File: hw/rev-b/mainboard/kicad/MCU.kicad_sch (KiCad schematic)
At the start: 34 parts, among them J23 MENU_HDR, SW4 RUN, SW5 MENU_BTN, U21 RP2040, Y1 12 MHz

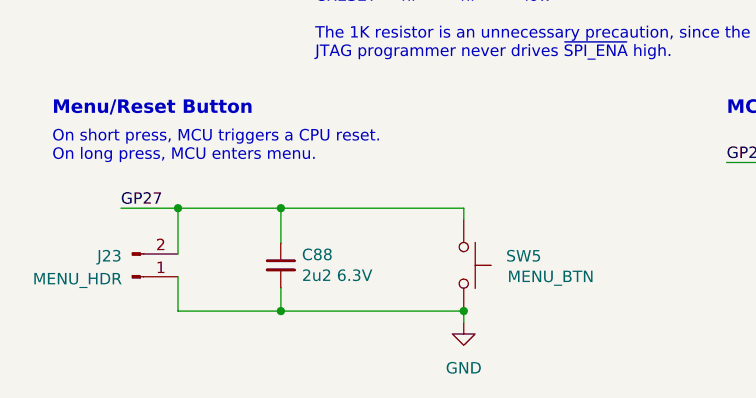
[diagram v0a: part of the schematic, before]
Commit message: hw: move USB-C for 8032SK (WIP)
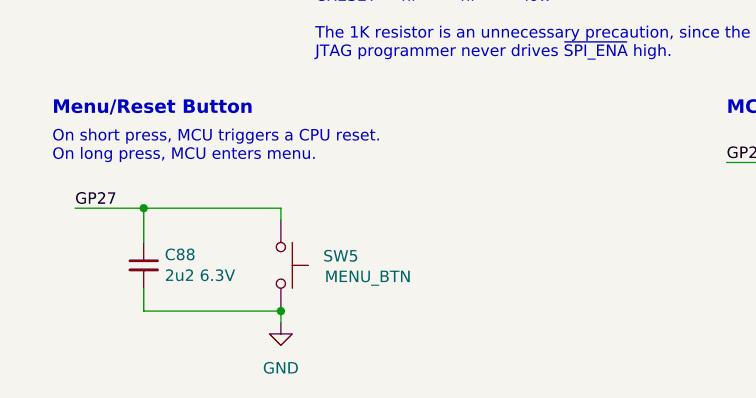
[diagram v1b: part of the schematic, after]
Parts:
- removed J23: MENU_HDR, Connector_PinHeader_2.54mm:PinHeader_1x02_P2.54mm_Vertical, symbol Connector:Conn_01x02_Pin
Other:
- moved on the sheet: C88, SW5
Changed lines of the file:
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@@
 	)
 	(junction
-		(at 44.45 179.07)
+		(at 29.21 179.07)
 		(diameter 0)
 		(color 0 0 0 0)
@@
 	)
 	(junction
-		(at 44.45 190.5)
-		(diameter 0)
-		(color 0 0 0 0)
-	)
-	(junction
 		(at 187.96 59.69)
 		(diameter 0)
@@
 	)
 	(junction
-		(at 64.77 190.5)
+		(at 44.45 190.5)
 		(diameter 0)
 		(color 0 0 0 0)
@@
 	)
 	(junction
-		(at 33.02 179.07)
-		(diameter 0)
-		(color 0 0 0 0)
-	)
-	(junction
 		(at 82.55 31.75)
 		(diameter 0)
@@
 	(wire
 		(pts
-			(xy 33.02 186.69) (xy 33.02 190.5)
-		)
-		(stroke
-			(width 0)
-			(type default)
-		)
-	)
-	(wire
-		(pts
 			(xy 193.04 52.07) (xy 193.04 53.34)
 		)
@@
 	(wire
 		(pts
-			(xy 33.02 190.5) (xy 44.45 190.5)
-		)
-		(stroke
-			(width 0)
-			(type default)
-		)
-	)
-	(wire
-		(pts
 			(xy 133.35 138.43) (xy 133.35 139.7)
 		)
@@
 	(wire
 		(pts
-			(xy 44.45 187.96) (xy 44.45 190.5)
+			(xy 29.21 187.96) (xy 29.21 190.5)
 		)
 		(stroke
@@
 	(wire
 		(pts
-			(xy 44.45 179.07) (xy 64.77 179.07)
+			(xy 29.21 179.07) (xy 44.45 179.07)
 		)
 		(stroke
@@
 	(wire
 		(pts
-			(xy 44.45 179.07) (xy 44.45 182.88)
+			(xy 29.21 179.07) (xy 29.21 182.88)
 		)
 		(stroke
@@
 	(wire
 		(pts
-			(xy 44.45 190.5) (xy 64.77 190.5)
+			(xy 29.21 190.5) (xy 44.45 190.5)
 		)
 		(stroke
@@
 	(wire
 		(pts
-			(xy 33.02 179.07) (xy 44.45 179.07)
+			(xy 21.59 179.07) (xy 29.21 179.07)
 		)
 		(stroke
@@
 	(wire
 		(pts
-			(xy 26.67 179.07) (xy 33.02 179.07)
-		)
-		(stroke
-			(width 0)
-			(type default)
-		)
-	)
-	(wire
-		(pts
 			(xy 71.12 95.25) (xy 82.55 95.25)
 		)
@@
 	(wire
 		(pts
-			(xy 64.77 190.5) (xy 64.77 191.77)
+			(xy 44.45 190.5) (xy 44.45 191.77)
 		)
 		(stroke
@@
 	(wire
 		(pts
-			(xy 64.77 179.07) (xy 64.77 180.34)
+			(xy 44.45 179.07) (xy 44.45 180.34)
 		)
 		(stroke
@@
 	(wire
 		(pts
-			(xy 33.02 179.07) (xy 33.02 184.15)
-		)
-		(stroke
-			(width 0)
-			(type default)
-		)
-	)
-	(wire
-		(pts
 			(xy 86.36 107.95) (xy 101.6 107.95)
 		)
@@
 	)
 	(label "GP27"
-		(at 26.67 179.07 0)
+		(at 21.59 179.07 0)
 		(fields_autoplaced yes)
 		(effects
@@
 	)
 	(symbol
-		(lib_id "Connector:Conn_01x02_Pin")
-		(at 27.94 186.69 0)
-		(mirror x)
-		(unit 1)
-		(exclude_from_sim no)
-		(in_bom yes)
-		(on_board yes)
-		(dnp no)
-		(property "Reference" "J23"
-			(at 25.4 184.404 0)
-			(effects
-				(font
-					(size 1.27 1.27)
-				)
-			)
-		)
-		(property "Value" "MENU_HDR"
-			(at 21.844 186.944 0)
-			(effects
-				(font
-					(size 1.27 1.27)
-				)
-			)
-		)
-		(property "Footprint" "Connector_PinHeader_2.54mm:PinHeader_1x02_P2.54mm_Vertical"
-			(at 27.94 186.69 0)
-			(effects
-				(font
-					(size 1.27 1.27)
-				)
-				(hide yes)
-			)
-		)
-		(property "Datasheet" "~"
-			(at 27.94 186.69 0)
-			(effects
-				(font
-					(size 1.27 1.27)
-				)
-				(hide yes)
-			)
-		)
-		(property "Description" "Generic connector, single row, 01x02, script generated"
-			(at 27.94 186.69 0)
-			(effects
-				(font
-					(size 1.27 1.27)
-				)
-				(hide yes)
-			)
-		)
-		(property "MOUSER" "649-1012937891002BLF"
-			(at 27.94 186.69 0)
-			(effects
-				(font
-					(size 1.27 1.27)
-				)
-				(hide yes)
-			)
-		)
-		(pin "1"
-		)
-		(pin "2"
-		)
-		(instances
-			(project ""
-				(path "/2eea20e6-112c-411a-b615-885ae773135a/00000000-0000-0000-0000-0000617d6918/b70241ab-8a5c-42d5-a1ab-8f4bc50a1197"
-					(reference "J23")
-					(unit 1)
-				)
-			)
-		)
-	)
-	(symbol
 		(lib_id "Device:C_Small")
 		(at 91.44 27.94 0)
@@
 	(symbol
 		(lib_id "Switch:SW_Push")
-		(at 64.77 185.42 270)
+		(at 44.45 185.42 270)
 		(mirror x)
 		(unit 1)
@@
 		(dnp no)
 		(property "Reference" "SW5"
-			(at 73.406 184.404 90)
+			(at 53.086 184.404 90)
 			(effects
 				(font
@@
 		)
 		(property "Value" "MENU_BTN"
-			(at 79.248 186.69 90)
+			(at 58.928 186.69 90)
 			(effects
 				(font
@@
 		)
 		(property "Footprint" "PET:APEM_MJTP1117"
-			(at 69.85 185.42 0)
+			(at 49.53 185.42 0)
 			(effects
 				(font
@@
 		)
 		(property "Datasheet" "https://www.mouser.com/datasheet/2/26/APPMS00088_1-2538152.pdf"
-			(at 69.85 185.42 0)
+			(at 49.53 185.42 0)
 			(effects
 				(font
@@
 		)
 		(property "Description" ""
-			(at 64.77 185.42 0)
+			(at 44.45 185.42 0)
 			(effects
 				(font
@@
 		)
 		(property "MOUSER" "642-MJTP1117"
-			(at 64.77 185.42 0)
+			(at 44.45 185.42 0)
 			(effects
 				(font
@@
 		)
 		(property "AliExpress" "https://www.aliexpress.us/item/2251832705063661.html"
-			(at 64.77 185.42 90)
+			(at 44.45 185.42 90)
 			(effects
 				(font
@@
 	(symbol
 		(lib_id "Device:C_Small")
-		(at 44.45 185.42 0)
+		(at 29.21 185.42 0)
 		(unit 1)
 		(exclude_from_sim no)
@@
 		(dnp no)
 		(property "Reference" "C88"
-			(at 46.7868 184.2516 0)
+			(at 31.5468 184.2516 0)
 			(effects
 				(font
@@
 		)
 		(property "Value" "2u2 6.3V"
-			(at 46.7868 186.563 0)
+			(at 31.5468 186.563 0)
 			(effects
 				(font
@@
 		)
 		(property "Footprint" "Capacitor_SMD:C_0402_1005Metric"
-			(at 44.45 185.42 0)
+			(at 29.21 185.42 0)
 			(effects
 				(font
@@
 		)
 		(property "Datasheet" "https://product.samsungsem.com/mlcc/CL05A225MQ5NSN.do"
-			(at 44.45 185.42 0)
+			(at 29.21 185.42 0)
 			(effects
 				(font
@@
 		)
 		(property "Description" ""
-			(at 44.45 185.42 0)
+			(at 29.21 185.42 0)
 			(effects
 				(font
@@
 		)
 		(property "LCSC" "C12530"
-			(at 44.45 185.42 0)
+			(at 29.21 185.42 0)
 			(effects
 				(font
@@
 	(symbol
 		(lib_id "power:GND")
-		(at 64.77 191.77 0)
+		(at 44.45 191.77 0)
 		(unit 1)
 		(exclude_from_sim no)
@@
 		(fields_autoplaced yes)
 		(property "Reference" "#PWR0151"
-			(at 64.77 198.12 0)
+			(at 44.45 198.12 0)
 			(effects
 				(font
@@
 		)
 		(property "Value" "GND"
-			(at 64.77 196.85 0)
+			(at 44.45 196.85 0)
 			(effects
 				(font
@@
 		)
 		(property "Footprint" ""
-			(at 64.77 191.77 0)
+			(at 44.45 191.77 0)
 			(effects
 				(font
@@
 		)
 		(property "Datasheet" ""
-			(at 64.77 191.77 0)
+			(at 44.45 191.77 0)
 			(effects
 				(font
@@
 		)
 		(property "Description" "Power symbol creates a global label with name \"GND\" , ground"
-			(at 64.77 191.77 0)
+			(at 44.45 191.77 0)
 			(effects
 				(font

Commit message: hw: many touch ups
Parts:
- added J23: MENU, Connector_PinHeader_2.54mm:PinHeader_1x02_P2.54mm_Vertical, symbol Connector:Conn_01x02_Pin
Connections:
- net GND: now also J23.1 (Pin_1)
- net GP27: now also J23.2 (Pin_2)
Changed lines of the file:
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@@
 	)
 	(junction
+		(at 44.45 179.07)
+		(diameter 0)
+		(color 0 0 0 0)
+	)
+	(junction
 		(at 182.88 33.02)
 		(diameter 0)
@@
 	)
 	(junction
-		(at 44.45 190.5)
+		(at 44.45 191.77)
 		(diameter 0)
 		(color 0 0 0 0)
@@
 	(wire
 		(pts
+			(xy 44.45 191.77) (xy 63.5 191.77)
+		)
+		(stroke
+			(width 0)
+			(type default)
+		)
+	)
+	(wire
+		(pts
 			(xy 60.96 80.01) (xy 71.12 80.01)
 		)
@@
 	(wire
 		(pts
-			(xy 165.1 77.47) (xy 237.49 77.47)
-		)
-		(stroke
-			(width 0)
-			(type default)
-		)
-	)
-	(wire
-		(pts
 			(xy 87.63 90.17) (xy 101.6 90.17)
 		)
@@
 	(wire
 		(pts
-			(xy 29.21 187.96) (xy 29.21 190.5)
+			(xy 29.21 187.96) (xy 29.21 191.77)
 		)
 		(stroke
@@
 	(wire
 		(pts
+			(xy 63.5 179.07) (xy 63.5 184.15)
+		)
+		(stroke
+			(width 0)
+			(type default)
+		)
+	)
+	(wire
+		(pts
 			(xy 132.08 35.56) (xy 132.08 36.83)
 		)
@@
 	(wire
 		(pts
+			(xy 44.45 179.07) (xy 63.5 179.07)
+		)
+		(stroke
+			(width 0)
+			(type default)
+		)
+	)
+	(wire
+		(pts
 			(xy 78.74 115.57) (xy 81.28 115.57)
 		)
@@
 	(wire
 		(pts
-			(xy 29.21 190.5) (xy 44.45 190.5)
+			(xy 29.21 191.77) (xy 44.45 191.77)
 		)
 		(stroke
@@
 	(wire
 		(pts
+			(xy 63.5 191.77) (xy 63.5 186.69)
+		)
+		(stroke
+			(width 0)
+			(type default)
+		)
+	)
+	(wire
+		(pts
 			(xy 218.44 146.05) (xy 246.38 146.05)
 		)
@@
 	(wire
 		(pts
+			(xy 224.79 77.47) (xy 237.49 77.47)
+		)
+		(stroke
+			(width 0)
+			(type default)
+		)
+	)
+	(wire
+		(pts
 			(xy 156.21 26.67) (xy 156.21 25.4)
 		)
@@
 	(wire
 		(pts
-			(xy 44.45 190.5) (xy 44.45 191.77)
+			(xy 44.45 191.77) (xy 44.45 193.04)
 		)
 		(stroke
@@
 	(wire
 		(pts
+			(xy 165.1 77.47) (xy 196.85 77.47)
+		)
+		(stroke
+			(width 0)
+			(type default)
+		)
+	)
+	(wire
+		(pts
 			(xy 246.38 130.81) (xy 246.38 146.05)
 		)
@@
 		)
 	)
+	(wire
+		(pts
+			(xy 44.45 191.77) (xy 44.45 190.5)
+		)
+		(stroke
+			(width 0)
+			(type default)
+		)
+	)
 	(text "100n at RUN pin\nfor EMI immunity.\nAvoids reset during\nCRT sync lock."
 		(exclude_from_sim no)
@@
 	)
 	(label "SD_DETECT"
-		(at 166.37 74.93 0)
+		(at 224.79 74.93 0)
 		(fields_autoplaced yes)
 		(effects
@@
 	)
 	(label "SD_~{CS}"
-		(at 166.37 77.47 0)
+		(at 224.79 77.47 0)
 		(fields_autoplaced yes)
 		(effects
@@
 		)
 	)
+	(hierarchical_label "SD_~{CS}"
+		(shape output)
+		(at 196.85 77.47 0)
+		(fields_autoplaced yes)
+		(effects
+			(font
+				(size 1.27 1.27)
+			)
+			(justify left)
+		)
+	)
 	(hierarchical_label "~{SPI_ENA}"
 		(shape input)
@@
 	)
 	(symbol
+		(lib_id "Connector:Conn_01x02_Pin")
+		(at 68.58 186.69 180)
+		(unit 1)
+		(exclude_from_sim no)
+		(in_bom yes)
+		(on_board yes)
+		(dnp no)
+		(fields_autoplaced yes)
+		(property "Reference" "J23"
+			(at 69.85 184.1499 0)
+			(effects
+				(font
+					(size 1.27 1.27)
+				)
+				(justify right)
+			)
+		)
+		(property "Value" "MENU"
+			(at 69.85 186.6899 0)
+			(effects
+				(font
+					(size 1.27 1.27)
+				)
+				(justify right)
+			)
+		)
+		(property "Footprint" "Connector_PinHeader_2.54mm:PinHeader_1x02_P2.54mm_Vertical"
+			(at 68.58 186.69 0)
+			(effects
+				(font
+					(size 1.27 1.27)
+				)
+				(hide yes)
+			)
+		)
+		(property "Datasheet" "~"
+			(at 68.58 186.69 0)
+			(effects
+				(font
+					(size 1.27 1.27)
+				)
+				(hide yes)
+			)
+		)
+		(property "Description" "Generic connector, single row, 01x02, script generated"
+			(at 68.58 186.69 0)
+			(effects
+				(font
+					(size 1.27 1.27)
+				)
+				(hide yes)
+			)
+		)
+		(property "MOUSER" "649-1012937891002BLF"
+			(at 68.58 186.69 0)
+			(effects
+				(font
+					(size 1.27 1.27)
+				)
+				(hide yes)
+			)
+		)
+		(pin "1"
+		)
+		(pin "2"
+		)
+		(instances
+			(project "Mainboard"
+				(path "/2eea20e6-112c-411a-b615-885ae773135a/00000000-0000-0000-0000-0000617d6918/b70241ab-8a5c-42d5-a1ab-8f4bc50a1197"
+					(reference "J23")
+					(unit 1)
+				)
+			)
+		)
+	)
+	(symbol
 		(lib_id "Jumper:SolderJumper_3_Open")
 		(at 218.44 151.13 270)
@@
 	(symbol
 		(lib_id "power:GND")
-		(at 44.45 191.77 0)
+		(at 44.45 193.04 0)
 		(unit 1)
 		(exclude_from_sim no)
@@
 		(fields_autoplaced yes)
 		(property "Reference" "#PWR0151"
-			(at 44.45 198.12 0)
+			(at 44.45 199.39 0)
 			(effects
 				(font
@@
 		)
 		(property "Value" "GND"
-			(at 44.45 196.85 0)
+			(at 44.45 198.12 0)
 			(effects
 				(font
@@
 		)
 		(property "Footprint" ""
-			(at 44.45 191.77 0)
+			(at 44.45 193.04 0)
 			(effects
 				(font
@@
 		)
 		(property "Datasheet" ""
-			(at 44.45 191.77 0)
+			(at 44.45 193.04 0)
 			(effects
 				(font
@@
 		)
 		(property "Description" "Power symbol creates a global label with name \"GND\" , ground"
-			(at 44.45 191.77 0)
+			(at 44.45 193.04 0)
 			(effects
 				(font

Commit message: chore(hw): tidy and set ${REVISION} to "B"
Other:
- company: https://is.gd/6hpvh6 -> https://tinyurl.com/econopet-rev-b
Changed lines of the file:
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@@
 	(title_block
 		(title "EconoPET 40/8096")
-		(date "2026-02-27")
-		(rev "B")
-		(company "https://is.gd/6hpvh6")
+		(date "2026-08-25")
+		(rev "${REVISION}")
+		(company "https://tinyurl.com/econopet-rev-b")
 		(comment 1 "Unspecified resistors are 1% / 62.5mW")
 		(comment 2 "Unspecified capacitors are 25V")

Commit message: chore(hw): tidy manufacturing files
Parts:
- SW4: value RUN -> TS-1088-AR02016; MOUSER 611-PTS636SK43LFS -> (none)
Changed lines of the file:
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@@
 			)
 		)
-		(property "Value" "RUN"
+		(property "Value" "TS-1088-AR02016"
 			(at 72.3392 123.063 90)
 			(effects
@@
 			)
 		)
-		(property "MOUSER" "611-PTS636SK43LFS"
+		(property "MOUSER" ""
 			(at 71.12 121.92 0)
 			(effects

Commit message: chore(hw): create production files
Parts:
- C3, C6, C90, C93, C94, C95, C96, C97, C98: LCSC C307331 -> (none); LCSC Part # (none) -> C307331
- C86, C87: LCSC C1562 -> (none); LCSC Part # (none) -> C1562
- C88, C91, C92: LCSC C12530 -> (none); LCSC Part # (none) -> C12530
- D11: LCSC C2986059 -> (none); LCSC Part # (none) -> C2986059
- R39: LCSC C25744 -> (none); LCSC Part # (none) -> C25744
- R40: LCSC C25900 -> (none); LCSC Part # (none) -> C25900
- R41, R42, R43: LCSC C11702 -> (none); LCSC Part # (none) -> C11702
- R44, R45, R48, R49: LCSC C25879 -> (none); LCSC Part # (none) -> C25879
- R46, R47: LCSC C25190 -> (none); LCSC Part # (none) -> C25190
- SW4: LCSC C720477 -> (none); LCSC Part # (none) -> C720477
- U21: LCSC C2040 -> (none); LCSC Part # (none) -> C2040
- Y1: LCSC C9002 -> (none); LCSC Part # (none) -> C9002

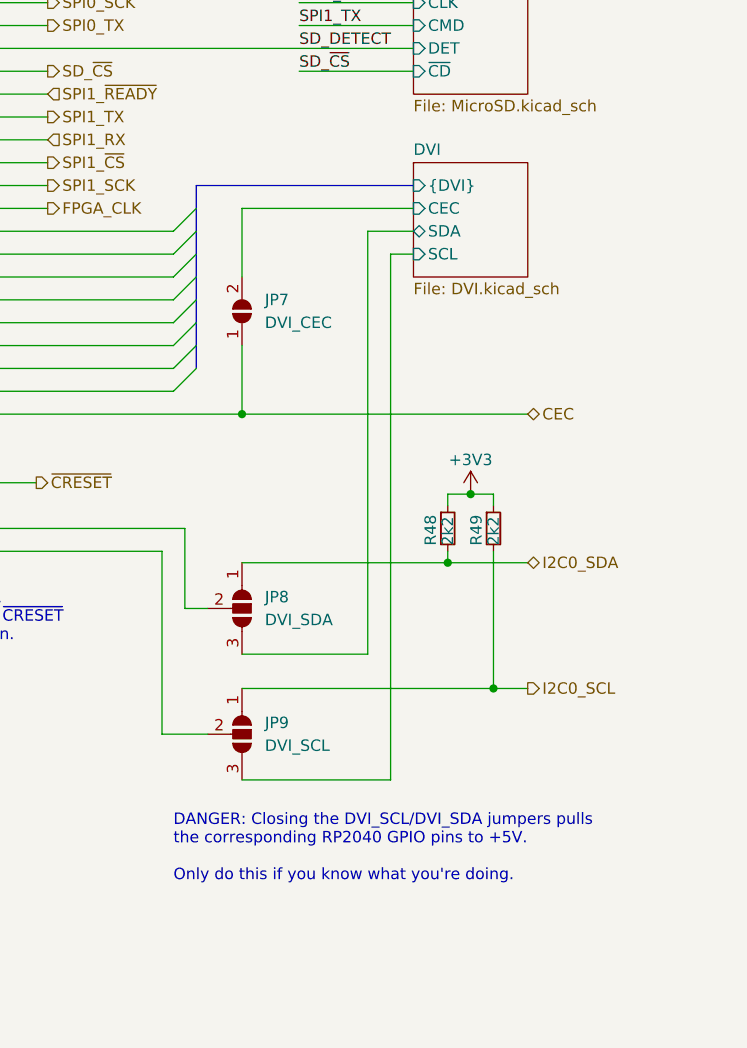
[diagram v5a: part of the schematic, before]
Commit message: fix(hw): remove I2C0 jumpers
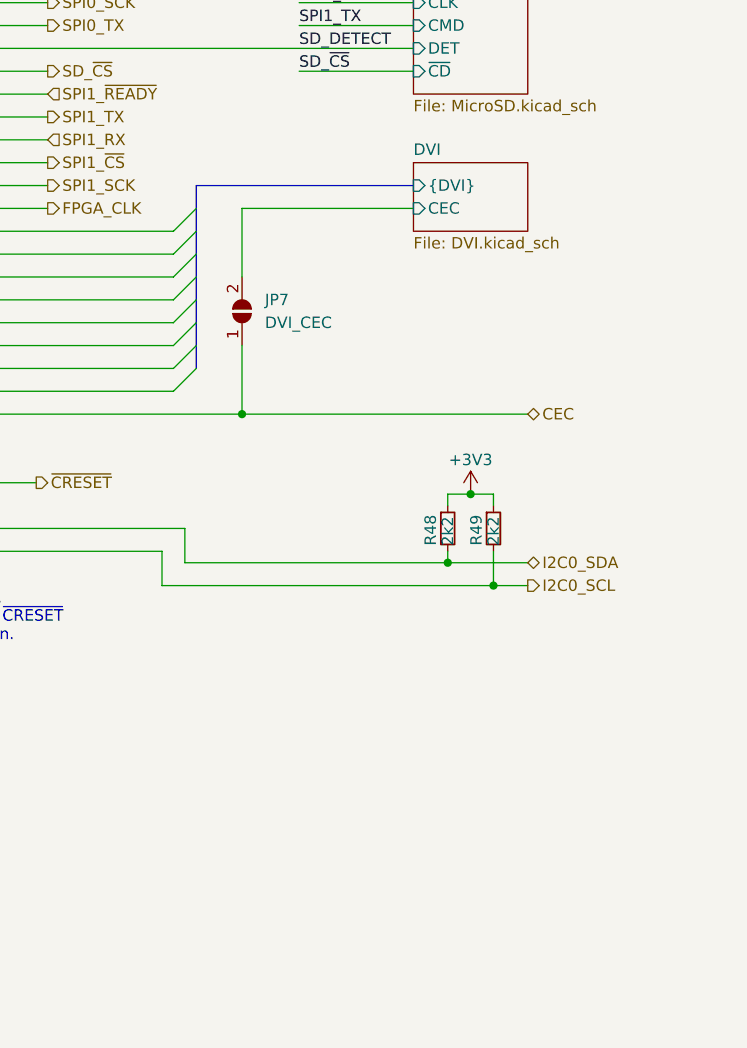
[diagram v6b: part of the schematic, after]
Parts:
- removed JP8: DVI_SDA, Jumper:SolderJumper-3_P1.3mm_Open_RoundedPad1.0x1.5mm, symbol Jumper:SolderJumper_3_Open
- removed JP9: DVI_SCL, Jumper:SolderJumper-3_P1.3mm_Open_RoundedPad1.0x1.5mm, symbol Jumper:SolderJumper_3_Open
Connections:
- net MCU_I2C0_SCL is gone; now on net I2C0_SCL: U21.41 (GPIO29_ADC3)
- net MCU_I2C0_SDA is gone; now on net I2C0_SDA: U21.40 (GPIO28_ADC2)
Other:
- sheet DVI ports: added none; removed SCL, SDA
- note removed: "DANGER: Closing the DVI_SCL/DVI_SDA jumpers pulls the corresponding RP2040 GPIO pins to +5V. Only do this if you know what you're doing."
